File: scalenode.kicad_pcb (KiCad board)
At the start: 4 copper layers, 173.5 x 40 mm, 161 parts, among them IC2 TPS2378DDA, J1 QSE-020-01-F-D, J2 QSE-020-01-F-D, J3 1-2199230-6, J4 1140084168, J5 0473460001, J6 SS-74800-144, J7 DF40HC(3.0)-100DS-0.4v, J8 DF40HC(3.0)-100DS-0.4v, M1 compute-module-4-1.5mm, Q1 MMBT3906,215, Q2 MMBT3906,215, Q3 SI7848BDP-T1-E3, Q4 SI7450DP-T1-GE3, Q5 MMBT3906,215, T1 P0926NL, T2 POE300F-50L, U1 TS3USB30EDGSR, U2 TPS62823DLCT, U3 UCC3809D2, U4 TCMT1107

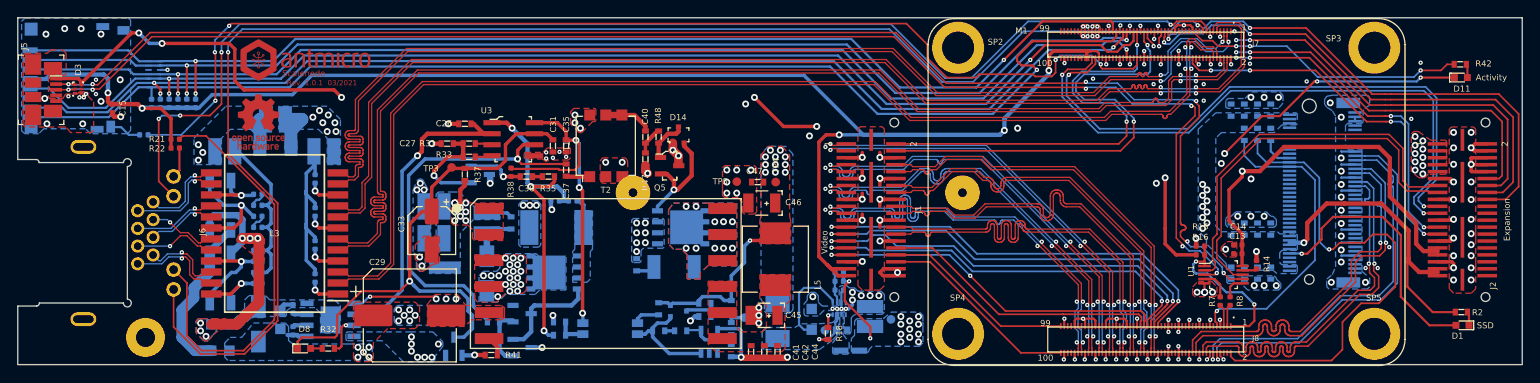
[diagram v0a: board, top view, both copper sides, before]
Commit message: Removed USB
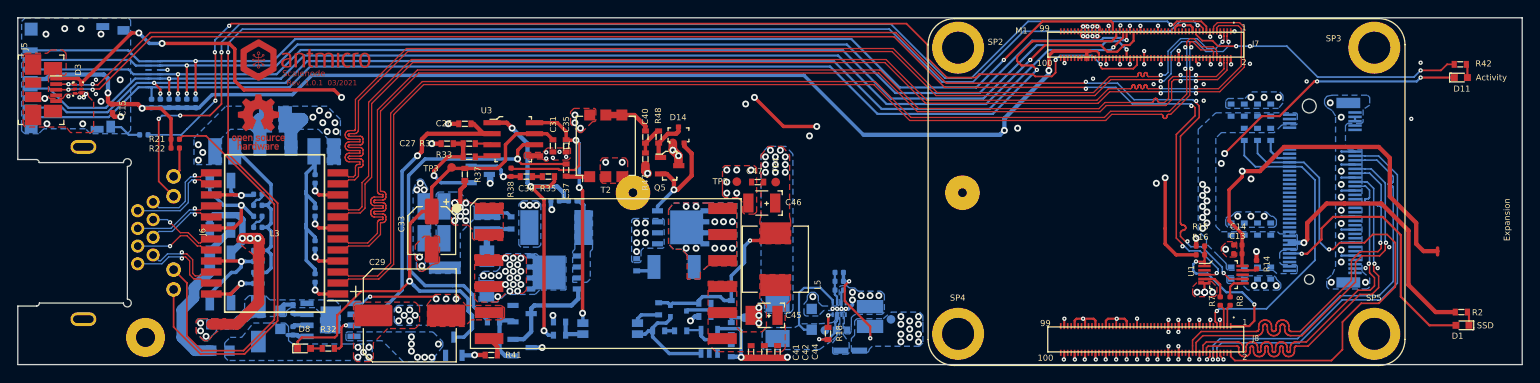
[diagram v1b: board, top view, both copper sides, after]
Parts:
- removed J1, J2: QSE-020-01-F-D, scalenode-footprints:QSE-020-01-XXX-D-A
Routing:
- net SDA0: track 70.1 -> 0.00 mm, vias 2 -> 0
- net SCL0: track 68.8 -> 0.00 mm, vias 2 -> 0
- net GPIO7: track 59.3 -> 0.00 mm, vias 2 -> 0
- net GPIO8: track 57.9 -> 0.00 mm, vias 2 -> 0
- net GPIO24: track 57.0 -> 0.00 mm, vias 3 -> 0
- net GPIO25: track 54.7 -> 0.00 mm, vias 3 -> 0
- net GPIO15: track 53.3 -> 0.00 mm, vias 2 -> 0
- net HDMI0_CK_N: track 51.1 -> 0.00 mm, vias 4 -> 0
- net HDMI0_CK_P: track 51.1 -> 0.00 mm, vias 4 -> 0
- net HDMI0_D0_N: track 50.7 -> 0.00 mm, vias 4 -> 0
- net HDMI0_D0_P: track 50.6 -> 0.00 mm, vias 4 -> 0
- net HDMI0_D2_P: track 50.5 -> 0.00 mm, vias 4 -> 0
- net HDMI0_D1_N: track 50.5 -> 0.00 mm, vias 4 -> 0
- net HDMI0_D1_P: track 50.4 -> 0.00 mm, vias 4 -> 0
- net GPIO14: track 50.3 -> 0.00 mm, vias 2 -> 0
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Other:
- net class Default removed
- net class Diff_100 removed
- net class Diff_90 removed
- board text removed: "Video"
